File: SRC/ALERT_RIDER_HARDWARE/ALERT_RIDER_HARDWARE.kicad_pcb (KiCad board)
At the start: 4 copper layers, 116 x 55.9 mm, 140 parts, among them J1 Screw_Terminal_01x02, J3 USB_C_Receptacle_USB2.0, J4 THERMISTOR, J8 Conn_01x06, Q1 IRLML5203TRPBF, Q2 DMP3056L-7, Q3 SK335N, Q4 SK335N, Q5 SK335N, Q6 IRLML0100TRPBF, Q7 DMP3056L-7, SW1 reset, SW2 GREEN, SW3 YELLOW, SW4 RED, SW5 CHANNEL, SW6 GREEN, U2 STM32F103C8Tx, U3 TPS63802DLAR, U4 MAX16150A, U5 LORA-E32-915T30S, U6 SM420561N, U7 MCP73833-AMI_UN, Y1 8MHz, Y2 32.678KHz

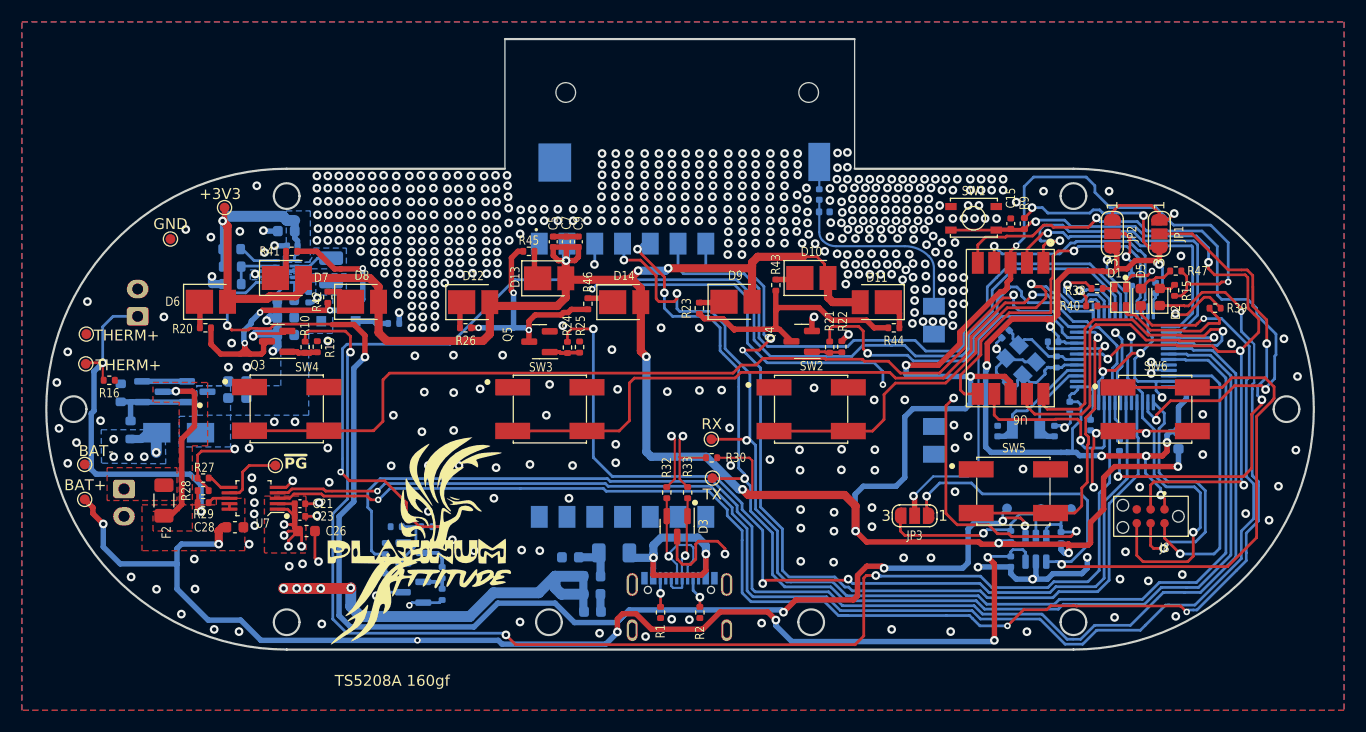
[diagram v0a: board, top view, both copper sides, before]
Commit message: complete Pa8-Pa7 LED placement maximized all files generated
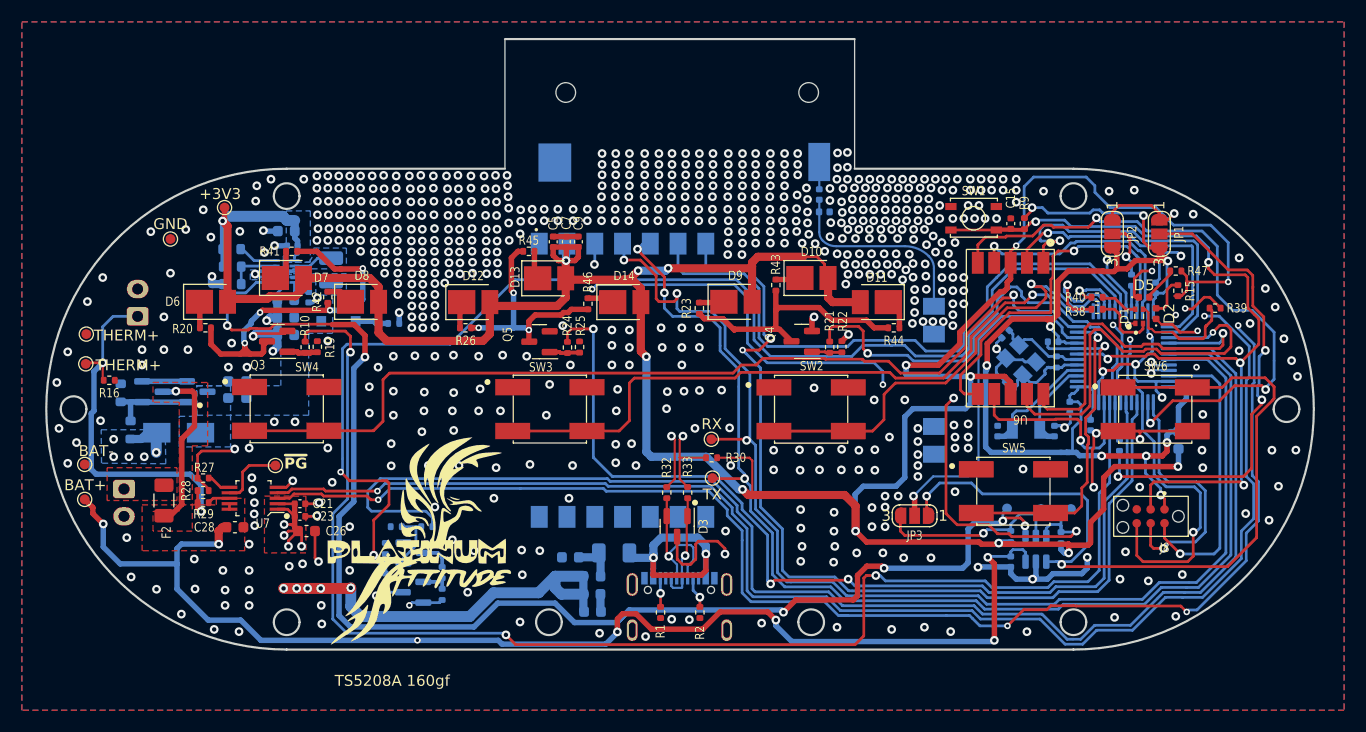
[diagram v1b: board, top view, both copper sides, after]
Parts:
- D1: value LED_KBGR -> LED_ARBG; footprint MACHADA_footprints:RCG_LED_606_TJ-S1615CY6TGLCCSRGB-A5 -> MACHADA_footprints:LED_APHF1608SEEQBDZGKC
- D2, D5: footprint LED_SMD:LED_0603_1608Metric -> LED_SMD:LED_0402_1005Metric
- moved D1 2.89 mm to (150.2, 59.0)
- moved R38 1.90 mm to (146.4, 58.3)
- moved D2 1.56 mm to (151.8, 58.7)
- moved R40 0.94 mm to (146.4, 57.2)
- moved R15 0.31 mm to (153.8, 56.6)
- moved D5 0.30 mm to (150.7, 57.2), turned to 0 degrees
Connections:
- D1 pad 1: GND -> /STM32F103C8_MCU/3v3_stm
- D1 pad 2: Net-(D1-BA) -> Net-(D1-RK)
- D1 pad 3: Net-(D1-GA) -> Net-(D1-BK)
- D1 pad 4: Net-(D1-RA) -> Net-(D1-GK)
- R38 pad 2: Net-(D1-RA) -> Net-(D1-RK)
- R39 pad 2: Net-(D1-BA) -> Net-(D1-BK)
- R40 pad 2: Net-(D1-GA) -> Net-(D1-GK)
- U2 pad 17: /bat_sense_en -> /BATTERY_VOLTAGE
- U2 pad 29: /BATTERY_VOLTAGE -> /bat_sense_en
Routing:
- net /bat_sense_en: track 111.4 -> 125.3 mm, vias 2 -> 0
- net /STM32F103C8_MCU/3v3_stm: track 102.6 -> 116.3 mm, vias 9 -> 11
- net Net-(D1-BA): track 11.9 -> 0.00 mm
- net /BATTERY_VOLTAGE: track 125.4 -> 113.7 mm, vias 0 -> 2
- net Net-(D1-BK): track 0.00 -> 10.7 mm
- net Net-(D1-RK): track 0.00 -> 5.95 mm
- net Net-(U2-PB14): track 30.9 -> 36.4 mm
- net Net-(D5-K): track 134.6 -> 139.5 mm, vias 2 -> 3
- net Net-(D1-GK): track 0.00 -> 3.45 mm
- net Net-(D2-A): track 1.49 -> 3.70 mm
- net /STM32F103C8_MCU/RGB_R: track 8.69 -> 10.3 mm
- net Net-(D2-K): track 134.9 -> 133.3 mm, vias 4 -> 5
- net Net-(D1-GA): track 1.61 -> 0.00 mm
- net GND: track 142.4 -> 143.6 mm, vias 592 -> 682
- net Net-(D1-RA): track 1.12 -> 0.00 mm
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
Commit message: complete update on production files and Design files
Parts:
- removed C11, C12, C13, C14: 22p, Capacitor_SMD:C_0402_1005Metric
- removed R7: 1M, Resistor_SMD:R_0402_1005Metric
- removed Y1: 8MHz, Crystal:Crystal_SMD_3225-4Pin_3.2x2.5mm
- removed Y2: 32.678KHz, Crystal:Crystal_SMD_3215-2Pin_3.2x1.5mm
- moved R39 12.9 mm to (144.7, 54.9)
- moved R40 0.60 mm to (146.4, 56.6)
- moved D2 0.41 mm to (151.4, 58.8)
- moved D1 0.16 mm to (150.1, 59.0)
- moved D5 0.10 mm to (150.7, 57.3)
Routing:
- net GND: track 143.6 -> 132.0 mm, vias 682 -> 702
- net /STM32F103C8_MCU/xtal_2: track 10.6 -> 0.00 mm
- net /STM32F103C8_MCU/xtal_1: track 8.40 -> 0.00 mm
- net /STM32F103C8_MCU/xtal_out: track 8.05 -> 0.00 mm
- net /STM32F103C8_MCU/xtal_in: track 7.95 -> 0.00 mm
- net /STM32F103C8_MCU/RGB_B: track 46.1 -> 43.2 mm
- net /STM32F103C8_MCU/3v3_stm: track 116.3 -> 117.7 mm
- net /STM32F103C8_MCU/BTN_~{CLR}: track 65.7 -> 67.1 mm
- net /STM32F103C8_MCU/RGB_G: track 5.58 -> 4.34 mm
- net Net-(D1-BK): track 10.7 -> 9.42 mm, vias 0 -> 1
- net Net-(U2-PB10): track 33.4 -> 34.0 mm

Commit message: alert rider updated complete internal rc HSI version
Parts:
- removed G***: LOGO, MYLOGOS:PLATINUM_SMALL
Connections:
- R15 pad 1: +3V3 -> +5V
- R47 pad 1: +3V3 -> +5V
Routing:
- net +5V: track 55.0 -> 167.0 mm, vias 14 -> 16
- net +3V3: track 291.7 -> 265.3 mm, vias 14 -> 13
- net /LEDS_W_DRIVERS2/INPUT: track 87.7 -> 110.9 mm, vias 3 -> 4
- net /BATTERY_VOLTAGE: track 113.7 -> 93.9 mm, vias 2 -> 3
- net /bat_sense_en: track 125.3 -> 109.4 mm, vias 0 -> 2
- net /STM32F103C8_MCU/PB4: track 86.9 -> 99.2 mm
- net /STM32F103C8_MCU/TX1: track 109.3 -> 118.2 mm
- net /STM32F103C8_MCU/RX1: track 110.6 -> 116.2 mm, vias 3 -> 4
- net /STM32F103C8_MCU/PB1: track 31.6 -> 35.0 mm
- net GND: track 132.0 -> 134.6 mm, vias 702 -> 700
- net /STM32F103C8_MCU/BTN_~{CLR}: track 67.1 -> 64.7 mm
- net /LEDS_W_DRIVERS1/INPUT: track 42.4 -> 44.4 mm, vias 1 -> 2
- net /STM32F103C8_MCU/PB3: track 56.9 -> 58.3 mm, vias 0 -> 2
- net /D+: track 57.4 -> 58.6 mm
- net /D-: track 55.7 -> 56.9 mm
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
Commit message: led update gerber placmenet
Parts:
- moved R44 4.75 mm to (123.2, 58.8)
- moved D11 0.55 mm to (126.8, 57.6), turned to 0 degrees
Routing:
- net Net-(Q4-D): track 24.3 -> 19.2 mm
- net +3V3: track 265.3 -> 268.1 mm
- net GND: vias 700 -> 699
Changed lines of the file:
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@@
     (property "ki_keywords" "R res resistor")
     (attr smd)
-    (fp_text reference "R22" (at -2.32 -0.09 90) (layer "F.SilkS")
+    (fp_text reference "R22" (at 0.07 -1.16 90) (layer "F.SilkS")
         (effects (font (size 0.85 0.7) (thickness 0.15)))
     )
@@
   )
   (footprint "Resistor_SMD:R_0402_1005Metric" (layer "F.Cu")
-    (at 127.8 60 180)
+    (at 123.2 58.8 180)
     (descr "Resistor SMD 0402 (1005 Metric), square (rectangular) end terminal, IPC_7351 nominal, (Body size source: IPC-SM-782 page 72, https://www.pcb-3d.com/wordpress/wp-content/uploads/ipc-sm-782a_amendment_1_and_2.pdf), generated with kicad-footprint-generator")
     (tags "resistor")
@@
     (property "ki_keywords" "R res resistor")
     (attr smd)
-    (fp_text reference "R44" (at 0 -1.17) (layer "F.SilkS")
+    (fp_text reference "R44" (at 0 -1.2) (layer "F.SilkS")
         (effects (font (size 0.85 0.7) (thickness 0.15)))
     )
@@
   )
   (footprint "LED_SMD:LED_PLCC_2835_Handsoldering" (layer "F.Cu")
-    (at 126.25 57.65 180)
+    (at 126.8 57.6)
     (descr "https://www.luckylight.cn/media/component/data-sheet/R2835BC-B2M-M10.pdf")
     (tags "LED")
@@
     (fp_line (start 1.75 1.4) (end -1.75 1.4)
       (stroke (width 0.1) (type solid)) (layer "F.Fab"))
-    (pad "1" smd rect (at -1.05 0 180) (size 2.5 2.2) (layers "F.Cu" "F.Paste" "F.Mask")
+    (pad "1" smd rect (at -1.05 0) (size 2.5 2.2) (layers "F.Cu" "F.Paste" "F.Mask")
       (net 93 "Net-(D11-K)") (pinfunction "K") (pintype "passive"))
-    (pad "2" smd rect (at 1.525 0 180) (size 1.55 2.2) (layers "F.Cu" "F.Paste" "F.Mask")
+    (pad "2" smd rect (at 1.525 0) (size 1.55 2.2) (layers "F.Cu" "F.Paste" "F.Mask")
       (net 3 "+3V3") (pinfunction "A") (pintype "passive"))
     (model "C:/Users/user/Documents/kicad6/KICAD 6.0.0/contractual_projects/ALERT_RIDER/ALERT_RIDER_HARDWARE/libs/3d_models/EAPL2835RA0.stp"
@@
     (property "ki_keywords" "R res resistor")
     (attr smd)
-    (fp_text reference "R21" (at -2.4 0.01 90) (layer "F.SilkS")
+    (fp_text reference "R21" (at 1.83 -0.27 -180) (layer "F.SilkS")
         (effects (font (size 0.85 0.7) (thickness 0.15)))
     )
@@
     (property "ki_keywords" "switch normally-open pushbutton push-button")
     (attr smd)
-    (fp_text reference "SW2" (at 0.05 -3.95) (layer "F.SilkS")
+    (fp_text reference "SW2" (at -3.03 -3.85) (layer "F.SilkS")
         (effects (font (size 0.85 0.7) (thickness 0.15)))
     )
@@
   (via (at 63.2 62) (size 0.8) (drill 0.4) (layers "F.Cu" "B.Cu") (free) (net 2))
   (via (at 88.05 52.06) (size 0.8) (drill 0.4) (layers "F.Cu" "B.Cu") (free) (net 2))
-  (via (at 129.7 57.5) (size 0.8) (drill 0.4) (layers "F.Cu" "B.Cu") (free) (net 2))
+  (via (at 129.870498 57.5) (size 0.8) (drill 0.4) (layers "F.Cu" "B.Cu") (free) (net 2))
   (via (at 102.41 75.64) (size 0.6) (drill 0.3) (layers "F.Cu" "B.Cu") (free) (net 2))
   (via (at 68.8 85.4) (size 0.8) (drill 0.4) (layers "F.Cu" "B.Cu") (free) (net 2))
@@
   (via (at 82.4 55) (size 0.8) (drill 0.4) (layers "F.Cu" "B.Cu") (free) (net 2))
   (via (at 116.5 50.2) (size 0.8) (drill 0.4) (layers "F.Cu" "B.Cu") (free) (net 2))
-  (via (at 129.7 56.5) (size 0.8) (drill 0.4) (layers "F.Cu" "B.Cu") (free) (net 2))
+  (via (at 129.8 56.4) (size 0.8) (drill 0.4) (layers "F.Cu" "B.Cu") (free) (net 2))
   (via (at 105 47) (size 0.8) (drill 0.4) (layers "F.Cu" "B.Cu") (free) (net 2))
   (via (at 65.6 87.6) (size 0.8) (drill 0.4) (layers "F.Cu" "B.Cu") (free) (net 2))
@@
   (via (at 125 48.2) (size 0.8) (drill 0.4) (layers "F.Cu" "B.Cu") (free) (net 2))
   (via (at 164.59 71.19) (size 0.8) (drill 0.4) (layers "F.Cu" "B.Cu") (free) (net 2))
-  (via (at 129.7 58.6) (size 0.8) (drill 0.4) (layers "F.Cu" "B.Cu") (free) (net 2))
+  (via (at 129.870498 58.6) (size 0.8) (drill 0.4) (layers "F.Cu" "B.Cu") (free) (net 2))
   (via (at 147.5 47.5) (size 0.8) (drill 0.4) (layers "F.Cu" "B.Cu") (free) (net 2))
   (via (at 88.05 50.98) (size 0.8) (drill 0.4) (layers "F.Cu" "B.Cu") (free) (net 2))
@@
   (via (at 139 48.5) (size 0.8) (drill 0.4) (layers "F.Cu" "B.Cu") (free) (net 2))
   (via (at 124 49.2) (size 0.8) (drill 0.4) (layers "F.Cu" "B.Cu") (free) (net 2))
-  (via (at 123.4 56) (size 0.8) (drill 0.4) (layers "F.Cu" "B.Cu") (free) (net 2))
   (via (at 90.44 48.47) (size 0.8) (drill 0.4) (layers "F.Cu" "B.Cu") (free) (net 2))
   (via (at 92 62.5) (size 0.8) (drill 0.4) (layers "F.Cu" "B.Cu") (free) (net 2))
@@
   (segment (start 114.825 55.59) (end 114.825 54.375) (width 0.75) (layer "F.Cu") (net 3))
   (segment (start 70.691726 57.115) (end 70.455226 57.3515) (width 0.75) (layer "F.Cu") (net 3))
-  (segment (start 124.725 57.65) (end 122.2 57.65) (width 0.75) (layer "F.Cu") (net 3))
   (segment (start 103.85 55.6) (end 103.1 55.6) (width 0.75) (layer "F.Cu") (net 3))
   (segment (start 138.485 55.515) (end 138.485 54.0525) (width 0.5) (layer "F.Cu") (net 3))
@@
   (segment (start 138.48 64.58) (end 138.39 64.49) (width 0.5) (layer "F.Cu") (net 3))
   (segment (start 70.455226 57.3515) (end 67.0935 57.3515) (width 0.75) (layer "F.Cu") (net 3))
+  (segment (start 127.15 55.95) (end 122.285 55.95) (width 0.5) (layer "F.Cu") (net 3))
   (segment (start 114.825 57.62) (end 114.825 55.59) (width 0.75) (layer "F.Cu") (net 3))
   (segment (start 137.863418 56.684) (end 138.177 56.370418) (width 0.5) (layer "F.Cu") (net 3))
   (segment (start 137.557838 56.684) (end 137.863418 56.684) (width 0.5) (layer "F.Cu") (net 3))
   (segment (start 97.775 57.225) (end 97.775 55.47) (width 0.75) (layer "F.Cu") (net 3))
-  (segment (start 121.775 57.225) (end 121.775 55.44) (width 0.75) (layer "F.Cu") (net 3))
-  (segment (start 122.2 57.65) (end 121.775 57.225) (width 0.75) (layer "F.Cu") (net 3))
   (segment (start 96.629 52.61) (end 97.829 52.61) (width 0.5) (layer "F.Cu") (net 3))
   (segment (start 81.4 61.2) (end 90.2 61.2) (width 0.75) (layer "F.Cu") (net 3))
   (segment (start 66.55 49) (end 66.55 50.05) (width 0.5) (layer "F.Cu") (net 3))
   (segment (start 79.84 55.44) (end 80.645 56.245) (width 0.75) (layer "F.Cu") (net 3))
+  (segment (start 128.325 57.6) (end 128.325 57.125) (width 0.5) (layer "F.Cu") (net 3))
   (segment (start 103.1 55.6) (end 103.5735 55.6) (width 0.75) (layer "F.Cu") (net 3))
   (segment (start 73.775 56.365) (end 73.025 57.115) (width 0.75) (layer "F.Cu") (net 3))
   (segment (start 80.645 56.245) (end 80.645 57.62) (width 0.75) (layer "F.Cu") (net 3))
+  (segment (start 122.285 55.95) (end 121.775 55.44) (width 0.5) (layer "F.Cu") (net 3))
   (segment (start 97 58) (end 97.775 57.225) (width 0.75) (layer "F.Cu") (net 3))
   (segment (start 104.645 59.4705) (end 104.645 57.65) (width 0.75) (layer "F.Cu") (net 3))
@@
   (segment (start 97.775 53.875) (end 97.8 53.85) (width 0.75) (layer "F.Cu") (net 3))
   (segment (start 108.2 56.2) (end 108.81 55.59) (width 0.75) (layer "F.Cu") (net 3))
+  (segment (start 128.325 57.125) (end 127.15 55.95) (width 0.5) (layer "F.Cu") (net 3))
   (segment (start 119.5 53.5) (end 120.78 53.5) (width 0.25) (layer "F.Cu") (net 3))
   (segment (start 80.645 57.62) (end 80.645 60.445) (width 0.75) (layer "F.Cu") (net 3))
@@
   (segment (start 121.97 62.24) (end 121.93 62.28) (width 0.254) (layer "F.Cu") (net 50))
   (segment (start 113.129965 60.129965) (end 112.17 59.17) (width 0.5) (layer "F.Cu") (net 51))
-  (segment (start 120.95 58.15) (end 117.25 58.15) (width 0.5) (layer "F.Cu") (net 51))
-  (segment (start 125.3 59.3) (end 122.1 59.3) (width 0.5) (layer "F.Cu") (net 51))
   (segment (start 117.322465 60.129965) (end 118.4325 61.24) (width 0.5) (layer "F.Cu") (net 51))
-  (segment (start 122.1 59.3) (end 120.95 58.15) (width 0.5) (layer "F.Cu") (net 51))
-  (segment (start 126 60) (end 125.3 59.3) (width 0.5) (layer "F.Cu") (net 51))
-  (segment (start 117.25 58.15) (end 117 58.4) (width 0.5) (layer "F.Cu") (net 51))
+  (segment (start 122.183274 58.8) (end 121.533274 58.15) (width 0.5) (layer "F.Cu") (net 51))
   (segment (start 116.8 60.129965) (end 117.322465 60.129965) (width 0.5) (layer "F.Cu") (net 51))
+  (segment (start 122.69 58.8) (end 122.183274 58.8) (width 0.5) (layer "F.Cu") (net 51))
+  (segment (start 121.533274 58.15) (end 117.25 58.15) (width 0.5) (layer "F.Cu") (net 51))
+  (segment (start 117.25 58.15) (end 117 58.4) (width 0.5) (layer "F.Cu") (net 51))
   (segment (start 116.8 60.129965) (end 113.129965 60.129965) (width 0.5) (layer "F.Cu") (net 51))
   (segment (start 117 58.4) (end 117 59.929965) (width 0.5) (layer "F.Cu") (net 51))
-  (segment (start 127.29 60) (end 126 60) (width 0.5) (layer "F.Cu") (net 51))
   (segment (start 117 59.929965) (end 116.8 60.129965) (width 0.5) (layer "F.Cu") (net 51))
   (segment (start 112.17 59.17) (end 110.46 59.17) (width 0.5) (layer "F.Cu") (net 51))
@@
   (segment (start 110 57.69) (end 112.18 57.69) (width 0.5) (layer "F.Cu") (net 92))
   (segment (start 112.18 57.69) (end 112.25 57.62) (width 0.5) (layer "F.Cu") (net 92))
-  (segment (start 128.31 58.66) (end 127.3 57.65) (width 0.5) (layer "F.Cu") (net 93))
-  (segment (start 128.31 60) (end 128.31 58.66) (width 0.5) (layer "F.Cu") (net 93))
+  (segment (start 125.75 57.791726) (end 125.75 57.6) (width 0.5) (layer "F.Cu") (net 93))
+  (segment (start 124.741726 58.8) (end 125.75 57.791726) (width 0.5) (layer "F.Cu") (net 93))
+  (segment (start 123.71 58.8) (end 124.741726 58.8) (width 0.5) (layer "F.Cu") (net 93))
   (segment (start 94.91 55.18) (end 95.2 55.47) (width 0.5) (layer "F.Cu") (net 94))
   (segment (start 94.91 53) (end 94.91 55.18) (width 0.5) (layer "F.Cu") (net 94))
